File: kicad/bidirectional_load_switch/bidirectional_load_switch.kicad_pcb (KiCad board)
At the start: 2 copper layers, 176.5 x 67.5 mm, 143 parts, among them J102 Conn_01x02_Socket, J103 Conn_01x09_Socket, J104 Conn_01x02_Socket, J105 Conn_01x02_Socket, J106 Conn_01x02_Socket, J107 AVR-ISP-6

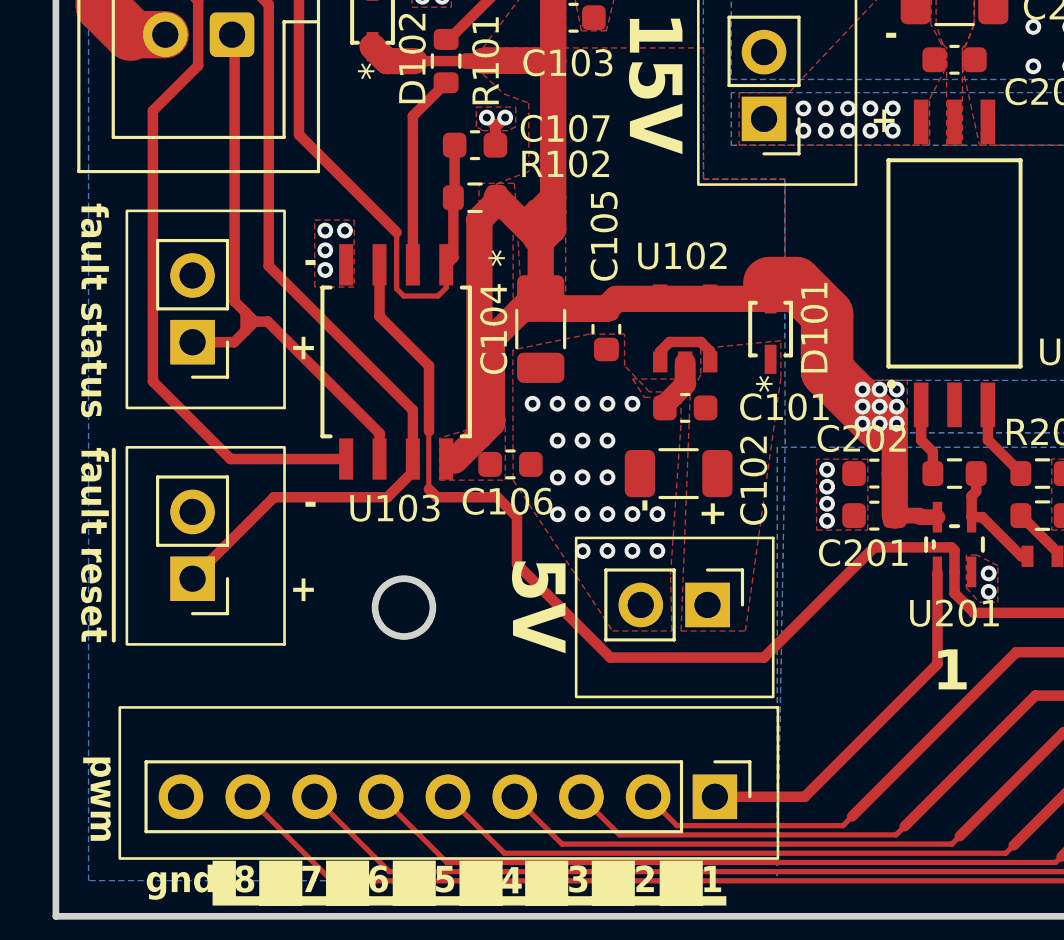
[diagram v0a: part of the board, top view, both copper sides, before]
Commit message: implementing 5v and 3v3 supply ORing
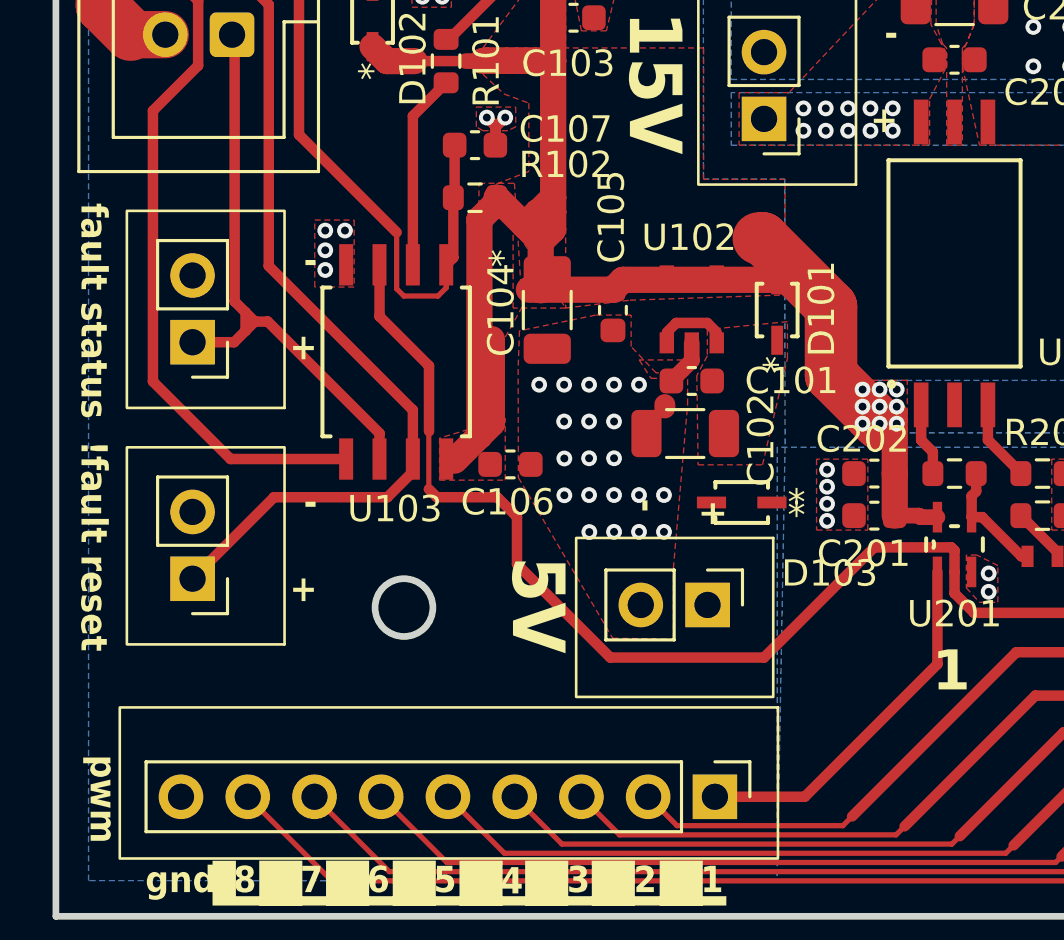
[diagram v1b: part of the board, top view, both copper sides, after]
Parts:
- added D103: ~, diode_CUS10S30_H3F:USC_TOS, F.Cu at (88.2, 112.9)
- moved C102 1.55 mm to (86.0, 110.3)
- moved C101 1.06 mm to (86.3, 108.3)
- moved C104 0.77 mm to (80.8, 105.6)
- moved C105 0.77 mm to (83.3, 105.6)
- moved D101 0.77 mm to (89.5, 105.6)
- moved U102 0.77 mm to (86.3, 105.5)
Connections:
- J102 pad 1: 5V -> Net-(J102-Pin_1)
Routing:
- net 3V3: track 107.3 -> 101.6 mm
- net 5V: track 3.05 -> 2.20 mm
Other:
- board text added: "!fault reset"
- board text removed: "~{fault reset}"

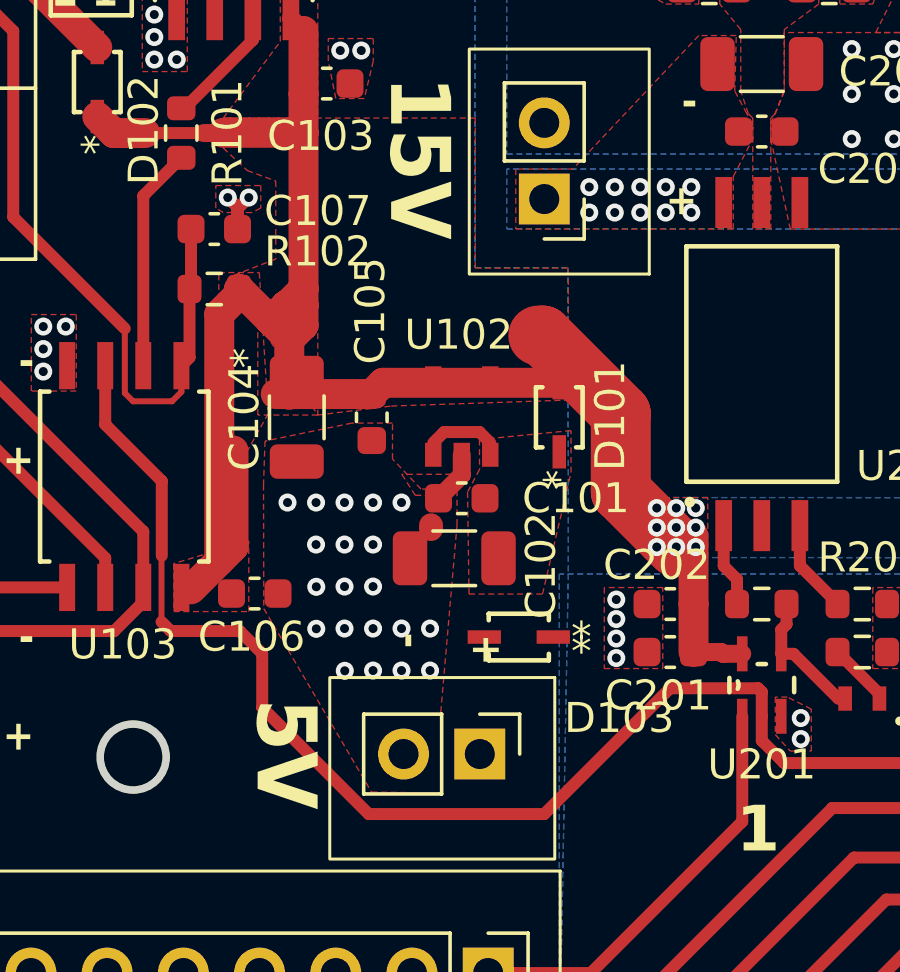
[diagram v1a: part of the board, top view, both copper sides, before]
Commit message: added 5v and 3v3 supply ORing and revised silkscreen text
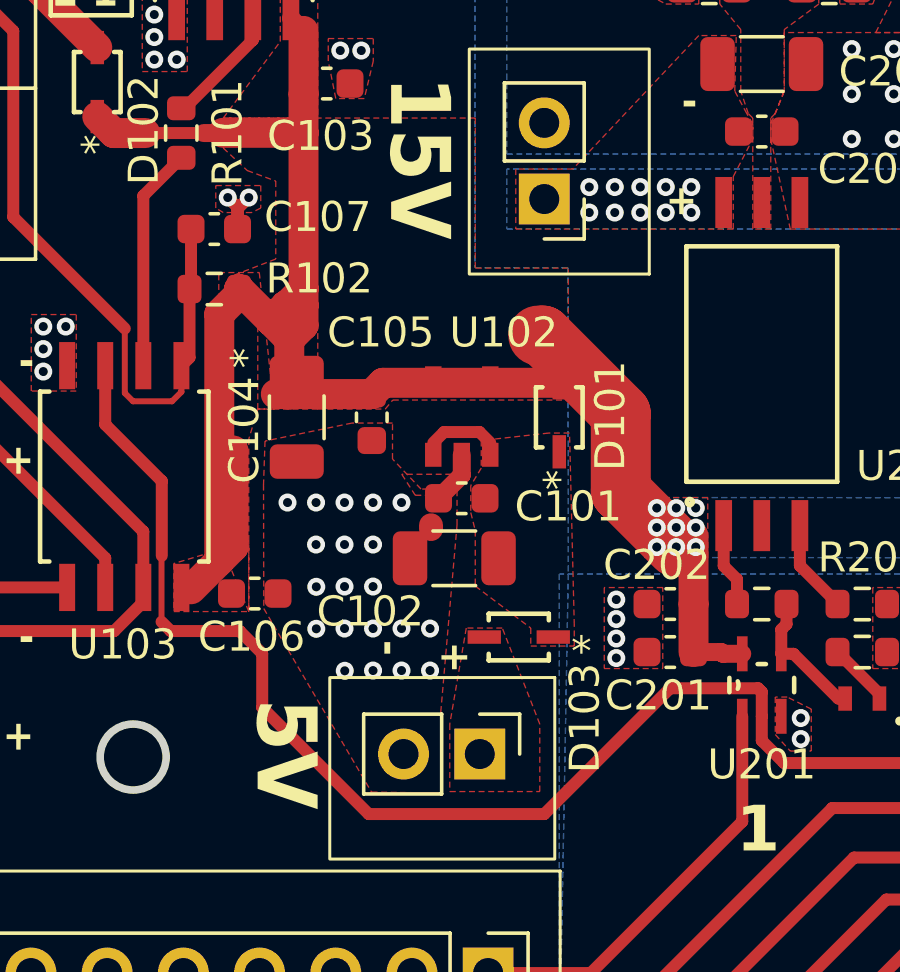
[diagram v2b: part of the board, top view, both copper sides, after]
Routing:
- added copper zone on F.Cu, net Net-(J102-Pin_1)
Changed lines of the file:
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@@
 		(tags "capacitor")
 		(property "Reference" "C102"
-			(at -2.8916 -0.2416 90)
+			(at 2.799998 -1.774999 0)
 			(layer "F.SilkS")
 			(effects
@@
 		(tags "resistor")
 		(property "Reference" "R102"
-			(at -3.45 1.25 0)
+			(at -3.5 0.35 0)
 			(layer "F.SilkS")
 			(effects
@@
 		(tags "capacitor")
 		(property "Reference" "C105"
-			(at -3.55 0.05 90)
+			(at -2.825001 -0.300002 180)
 			(layer "F.SilkS")
 			(effects
@@
 		(tags "CUS10S30_H3F ")
 		(property "Reference" "D103"
-			(at -3.35 -2.7 0)
+			(at -2.2 -2.7 90)
 			(unlocked yes)
 			(layer "F.SilkS")
@@
 		)
 		(property "Footprint" "diode_CUS10S30_H3F:USC_TOS"
-			(at 0 0 360)
+			(at 0 0 0)
 			(layer "F.Fab")
 			(hide yes)
@@
 		)
 		(property "Datasheet" "https://toshiba.semicon-storage.com/info/CUS10S30_datasheet_en_20140407.pdf?did=14077&prodName=CUS10S30"
-			(at 0 0 360)
+			(at 0 0 0)
 			(layer "F.Fab")
 			(hide yes)
@@
 		)
 		(property "Description" ""
-			(at 0 0 360)
+			(at 0 0 0)
 			(layer "F.Fab")
 			(hide yes)
@@
 		)
 		(fp_text user "*"
-			(at -2.0866 0 360)
-			(layer "F.SilkS")
-			(effects
-				(font
-					(size 1 1)
-					(thickness 0.15)
-				)
-			)
-		)
-		(fp_text user "*"
 			(at -2.0866 0 180)
 			(unlocked yes)
@@
 			)
 		)
-		(fp_text user "*"
-			(at -0.621 0 180)
+		(fp_text user "${REFERENCE}"
+			(at 0 0 180)
 			(unlocked yes)
 			(layer "F.Fab")
@@
 		)
 		(fp_text user "*"
-			(at -0.621 0 360)
+			(at -0.621 0 180)
+			(unlocked yes)
 			(layer "F.Fab")
 			(effects
@@
 			)
 		)
-		(fp_text user "${REFERENCE}"
-			(at 0 0 180)
+		(fp_text user "*"
+			(at -0.621 0 180)
 			(unlocked yes)
 			(layer "F.Fab")
@@
 		(tags "capacitor")
 		(property "Reference" "C107"
-			(at 3.45 -0.6 0)
+			(at 3.45 -0.4 0)
 			(layer "F.SilkS")
 			(effects
@@
 		(tags "TLV75733PDBVR ")
 		(property "Reference" "U102"
-			(at 2.724999 -0.100002 0)
+			(at 2.8 1.4 0)
 			(unlocked yes)
 			(layer "F.SilkS")
@@
 		(fp_arc
 			(start 0.723714 -1.445998)
-			(mid 0.77694 -1.423891)
+			(mid 0.776959 -1.423902)
 			(end 0.799455 -1.37084)
 			(stroke
@@
 		(tags "capacitor")
 		(property "Reference" "C101"
-			(at -3.8 0 0)
+			(at -3.550002 -0.274999 0)
 			(layer "F.SilkS")
 			(effects
@@
 		(tags "capacitor")
 		(property "Reference" "C104"
-			(at 0 1.75 90)
+			(at 0.424999 1.75 90)
 			(layer "F.SilkS")
 			(effects
@@
 	)
 	(gr_text "-"
-		(at 84 112.75 270)
+		(at 83.3 113 270)
 		(layer "F.SilkS")
 		(effects
@@
 	)
 	(gr_text "+"
-		(at 86.55 112.8 270)
+		(at 85.5 113.05 270)
 		(layer "F.SilkS")
 		(effects
@@
 	)
 	(zone
+		(net 98)
+		(net_name "Net-(J102-Pin_1)")
+		(layer "F.Cu")
+		(hatch edge 0.5)
+		(priority 22)
+		(connect_pads yes
+			(clearance 0.1524)
+		)
+		(min_thickness 0.25)
+		(filled_areas_thickness no)
+		(fill yes
+			(thermal_gap 0.5)
+			(thermal_bridge_width 0.5)
+		)
+		(polygon
+			(pts
+				(xy 85.9 118.05) (xy 88.9 118.05) (xy 88.9 115.8) (xy 87.65 112.6) (xy 86.45 112.6) (xy 85.9 115.8)
+			)
+		)
+	)
+	(zone
 		(net 2)
 		(net_name "GND")
@@
 		(polygon
 			(pts
-				(xy 79.5 105.5) (xy 79.5 102.45) (xy 81.5 102.45) (xy 81.5 105.5)
+				(xy 79.5 105.3) (xy 79.5 102.45) (xy 81.5 102.45) (xy 81.5 105.3)
 			)
 		)
@@
 		(polygon
 			(pts
-				(xy 86.541598 111.466601) (xy 88.991598 111.466601) (xy 89.941598 107.416601) (xy 89.941598 106.016601)
-				(xy 86.891598 106.316601) (xy 86.891598 107.316601) (xy 86.491598 108.066601)
+				(xy 86.6 108.75) (xy 86.75 109.35) (xy 86.75 111.2) (xy 88.6 112.6) (xy 88.6 113.2) (xy 90.05 113.2)
+				(xy 90.05 112.5) (xy 89.891598 106.1) (xy 89.2 106.1) (xy 86.95 106.35) (xy 86.95 107.266601) (xy 86.6 107.85)
 			)
 		)
@@
 		(polygon
 			(pts
-				(xy 78.35 96.6) (xy 79.15 97.35) (xy 80.1 97.7) (xy 80.1 100.3) (xy 78.55 100.9) (xy 81.5 105.5)
-				(xy 83.95 105.2) (xy 89.85 105) (xy 89.85 100.6) (xy 86.75 100.6) (xy 86.75 95.6) (xy 78.35 95.6)
+				(xy 78.35 96.6) (xy 79.15 97.35) (xy 80.1 97.7) (xy 80.1 100.3) (xy 78.55 100.9) (xy 81.5 105.3)
+				(xy 83.75 105.3) (xy 84 105) (xy 89.85 105) (xy 89.85 100.6) (xy 86.75 100.6) (xy 86.75 95.6) (xy 78.35 95.6)
 			)
 		)
@@
 		(polygon
 			(pts
-				(xy 78.2 109.65) (xy 78.2 100.75) (xy 79.55 100.75) (xy 79.85 105.45) (xy 79.15 106.7)
+				(xy 79.2 112.05) (xy 78.2 109.65) (xy 78.2 100.75) (xy 79.55 100.75) (xy 80.05 105.3) (xy 79.5 105.3)
+				(xy 79.2 106.3)
 			)
 		)

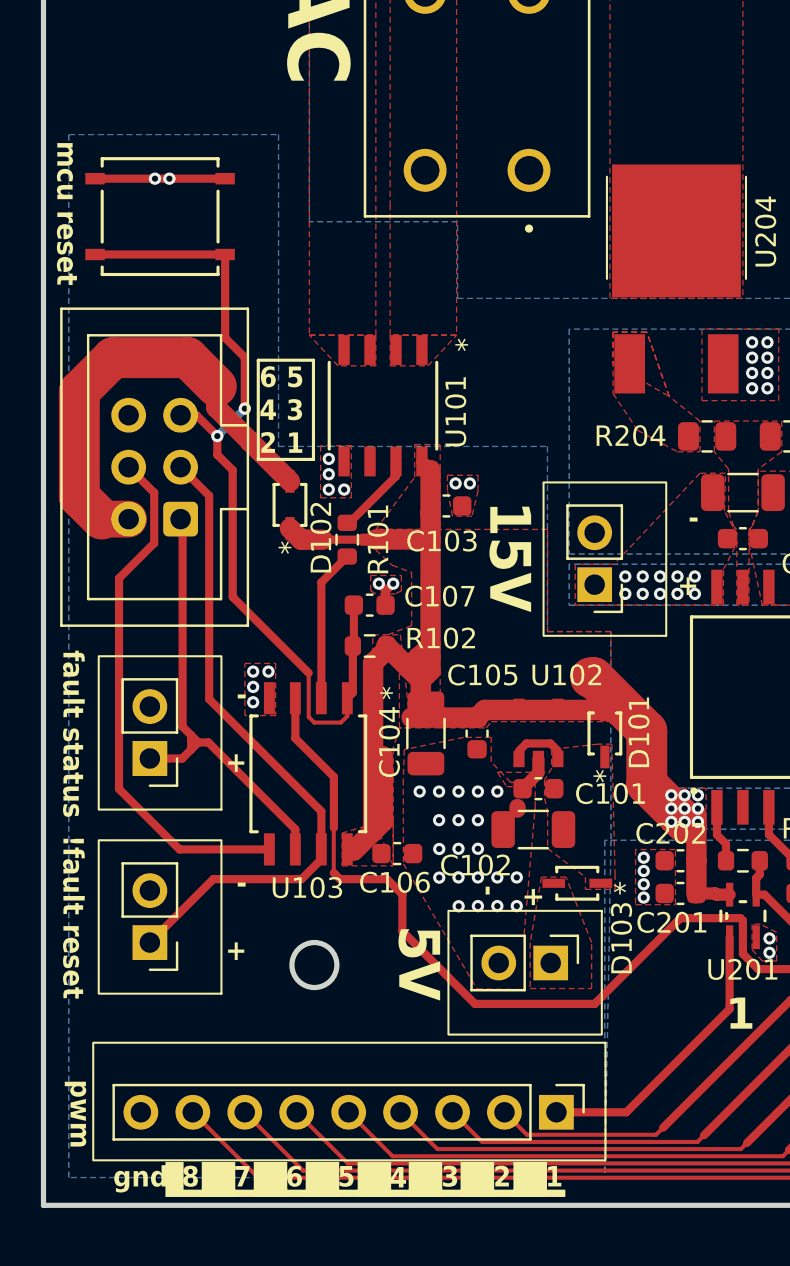
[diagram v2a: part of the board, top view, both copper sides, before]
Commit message: improved load switch mosfet paste aperture
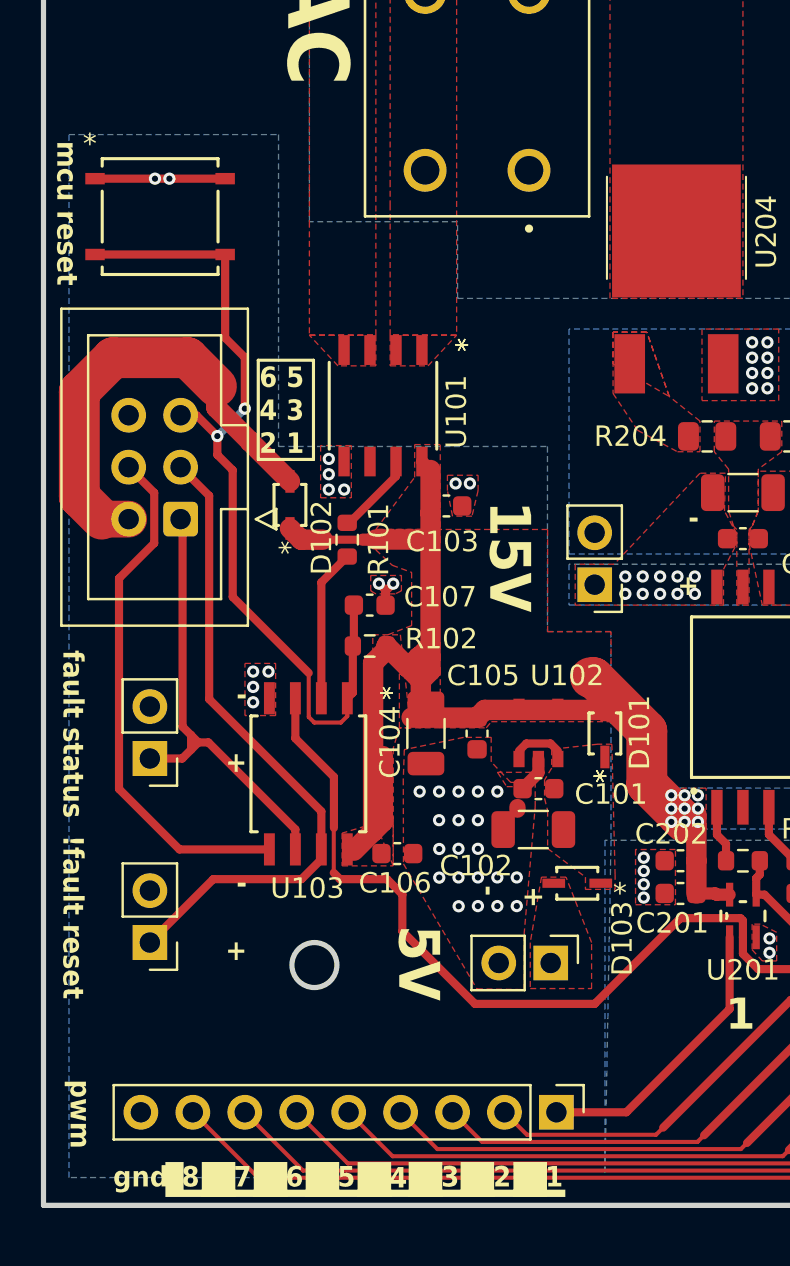
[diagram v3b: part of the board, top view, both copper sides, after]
